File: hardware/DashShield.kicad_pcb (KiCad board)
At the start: 2 copper layers, 112 parts, among them J001 PWR, J101 CAN0, J202 CAN1, J3 Dash LEDs, J301 Steering Wheel, J601 GPIO, Q301 2N7002, Q302 2N7002, Q303 2N7002, Q501 2N7002, Q502 2N7002, Q503 2N7002, Q504 2N7002, Q505 2N7002, Q506 2N7002, U101 MCP2515-xST, U102 MCP2562-E-SN, U201 MCP2515-xST, U202 MCP2562-E-SN, U401 CAT24C256, Y101 8MHz, Y201 8MHz

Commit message: chore: upload progress
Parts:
- added H601: MH, MountingHole:MountingHole_2.7mm_M2.5_Pad, F.Cu at (159.5, 100.0)
- added H602: MH, MountingHole:MountingHole_2.7mm_M2.5_Pad, F.Cu at (217.5, 100.0)
- added H603: MH, MountingHole:MountingHole_2.7mm_M2.5_Pad, F.Cu at (217.5, 149.0)
- added H604: MH, MountingHole:MountingHole_2.7mm_M2.5_Pad, F.Cu at (159.5, 149.0)
- C102, C103, C202, C203: value 22pF -> 16pF
- J601, U101, U102, U201, U202: moved to B.Cu
- Y101, Y201: footprint Crystal:Crystal_SMD_HC49-SD -> Crystal:Crystal_C38-LF_D3.0mm_L8.0mm_Vertical
- moved C105 176.8 mm to (263.0, 145.9), turned to -90 degrees
- moved R104 173.2 mm to (263.8, 141.5), turned to 90 degrees
- moved R103 169.4 mm to (255.8, 147.1)
- moved JP101 163.4 mm to (261.2, 141.2), turned to -90 degrees
- moved JP102 155.6 mm to (258.7, 137.4), turned to 90 degrees
- moved C203 147.7 mm to (234.4, 125.7), turned to -90 degrees
- moved R305 141.6 mm to (210.7, 160.7), turned to -90 degrees
- moved R201 140.8 mm to (225.6, 147.6), turned to 180 degrees
- moved C202 140.5 mm to (232.9, 125.7), turned to 90 degrees
- moved R202 140.3 mm to (225.6, 149.1)
- moved R306 137.8 mm to (210.0, 158.5)
- moved R307 133.8 mm to (204.6, 160.7), turned to 90 degrees
- moved R308 133.1 mm to (206.2, 160.7), turned to -90 degrees
- moved R309 129.3 mm to (205.4, 158.5)
- moved R304 126.0 mm to (209.2, 160.7), turned to 90 degrees
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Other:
- board outline added: 65 x 56.5 mm
- copper layers 2 -> 4

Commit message: Chore-Upload progress
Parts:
- JP101, JP102, JP201, JP202: footprint Connector_PinHeader_2.54mm:PinHeader_1x02_P2.54mm_Vertical -> Jumper:SolderJumper-2_P1.3mm_Open_RoundedPad1.0x1.5mm
- JP401: renamed from JP1; footprint Connector_PinHeader_2.54mm:PinHeader_1x02_P2.54mm_Vertical -> Jumper:SolderJumper-2_P1.3mm_Open_RoundedPad1.0x1.5mm
- moved C104 126.3 mm to (208.0, 142.5), turned to 90 degrees
- moved C101 121.6 mm to (205.5, 129.8), turned to 180 degrees
- moved R13 121.2 mm to (200.1, 137.4), turned to 180 degrees
- moved C401 116.3 mm to (205.4, 121.2)
- moved C205 116.1 mm to (190.5, 141.2), turned to 180 degrees
- moved C201 115.2 mm to (197.6, 143.5), turned to 90 degrees
- moved C204 114.7 mm to (191.0, 135.9), turned to 180 degrees
- moved R204 104.3 mm to (187.2, 144.0), turned to 90 degrees
- moved JP401 96.8 mm to (192.8, 120.5), turned to -90 degrees
- moved R403 94.1 mm to (200.9, 121.2), turned to 180 degrees
- moved R401 90.2 mm to (197.3, 114.6)
- moved R402 90.1 mm to (197.3, 116.8)
- moved C005 83.1 mm to (179.1, 123.7)
- moved C001 79.1 mm to (171.2, 121.7)
- moved C006 79.0 mm to (186.2, 115.6), turned to -90 degrees
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
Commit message: rev2
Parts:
- removed D007: LED, LED_SMD:LED_0603_1608Metric
- added C301: 10nF, Capacitor_SMD:C_0603_1608Metric, F.Cu at (164.4, 133.3)
- added C302: 10nF, Capacitor_SMD:C_0603_1608Metric, F.Cu at (168.3, 136.6)
- added C601: 100nF, Capacitor_SMD:C_0603_1608Metric, F.Cu at (171.3, 134.1)
- added C602: 10nF, Capacitor_SMD:C_0603_1608Metric, F.Cu at (171.3, 130.9)
- added J002: Data Logger, Connector_Molex:Molex_Micro-Fit_3.0_43650-0315_1x03_P3.00mm_Vertical, F.Cu at (189.3, 149.2)
- added U601: ADS1015IDGS, Package_SO:TSSOP-10_3x3mm_P0.5mm, F.Cu at (168.5, 132.6)
- D001, D005: value PMEG3050 -> PMEG100V080ELPD; footprint Diode_SMD:D_SOD-128 -> Package_TO_SOT_SMD:Nexperia_CFP15_SOT-1289
- D006: value PMEG3050 -> LED; footprint Diode_SMD:D_SOD-128 -> LED_SMD:LED_0603_1608Metric
- moved R318 46.7 mm to (157.6, 144.4)
- moved R321 42.0 mm to (157.6, 140.4)
- moved R324 37.2 mm to (157.6, 136.4)
- moved JP201 27.4 mm to (206.8, 144.2)
- moved JP202 24.5 mm to (209.8, 144.2)
- moved J101 23.1 mm to (217.7, 130.6), turned to 90 degrees
- moved R201 20.6 mm to (215.3, 138.8), turned to 0 degrees
- moved C008 20.0 mm to (186.2, 129.1)
- moved R202 19.4 mm to (215.3, 140.6), turned to 180 degrees
- moved U201 18.4 mm to (215.9, 139.7), turned to -90 degrees
- moved R13 18.0 mm to (216.3, 145.2)
- moved Y201 17.7 mm to (211.5, 140.7), turned to 90 degrees
- moved R511 17.6 mm to (209.7, 114.9)
- moved C202 17.6 mm to (211.5, 136.1), turned to 90 degrees
- moved R204 16.6 mm to (203.8, 144.4)
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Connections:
- C003 pad 1: /GPIO3/SCL1 -> /VIN Sense
- C004 pad 1: /GPIO2/SDA1 -> /VBATT Sense
- D001 pad 1: VS -> Net-(J001-Pin_1)
- D001 pad 2: Net-(D001-A) -> Net-(J001-Pin_1)
- D005 pad 1: VS -> +BATT
- D006 pad 1: VS -> GND
- D006 pad 2: +BATT -> Net-(D006-A)
- J001 pad 1: Net-(D001-A) -> Net-(J001-Pin_1)
- R004 pad 1: Net-(D007-A) -> Net-(D006-A)
- R005 pad 1: /GPIO3/SCL1 -> /VIN Sense
- R006 pad 2: /GPIO3/SCL1 -> /VIN Sense
- R007 pad 1: /GPIO2/SDA1 -> /VBATT Sense
- R008 pad 2: /GPIO2/SDA1 -> /VBATT Sense
- R312 pad 1: /GPIO18/PCM.CLK -> /Wheel Slip Adjust
- R315 pad 1: /GPIO23 -> /TC Power Adjust
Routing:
- net GND: track 0.00 -> 129.8 mm, vias 0 -> 23
- net /GPIO10/SPI0.MOSI: track 0.00 -> 82.4 mm
- net /CAN1 INT: track 0.00 -> 81.0 mm, vias 0 -> 1
- net /GPIO11/SPI0.SCLK: track 0.00 -> 69.6 mm, vias 0 -> 2
- net /GPIO9/SPI0.MISO: track 0.00 -> 65.3 mm, vias 0 -> 2
- net /GPIO22: track 0.00 -> 58.9 mm, vias 0 -> 1
- net /GPIO21/PCM.DOUT: track 0.00 -> 58.1 mm, vias 0 -> 1
- net /VIN Sense: track 0.00 -> 57.7 mm, vias 0 -> 4
- net /GPIO7/SPI0.CE1: track 0.00 -> 57.2 mm, vias 0 -> 2
- net /GPIO27: track 0.00 -> 54.2 mm, vias 0 -> 1
- net /GPIO16: track 0.00 -> 53.3 mm, vias 0 -> 1
- net /GPIO20/PCM.DIN: track 0.00 -> 52.5 mm, vias 0 -> 1
- net /CAN0 INT: track 0.00 -> 50.0 mm, vias 0 -> 1
- net /GPIO17: track 0.00 -> 46.9 mm, vias 0 -> 1
- net /GPIO3/SCL1: track 0.00 -> 38.9 mm, vias 0 -> 1
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- added copper zone on In2.Cu, net +5V
- added copper zone on In1.Cu, net GND

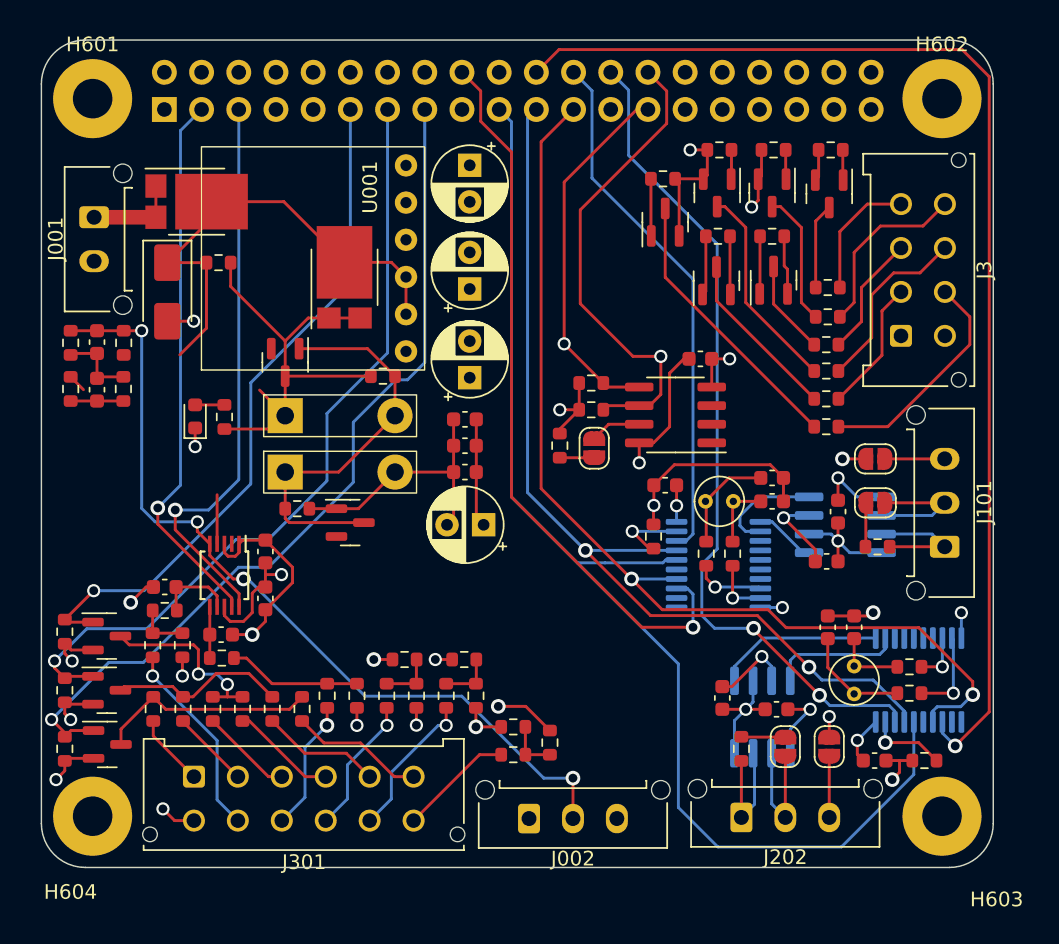
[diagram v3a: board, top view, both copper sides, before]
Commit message: feat: added pours & pass-through for CAN0&CAN1
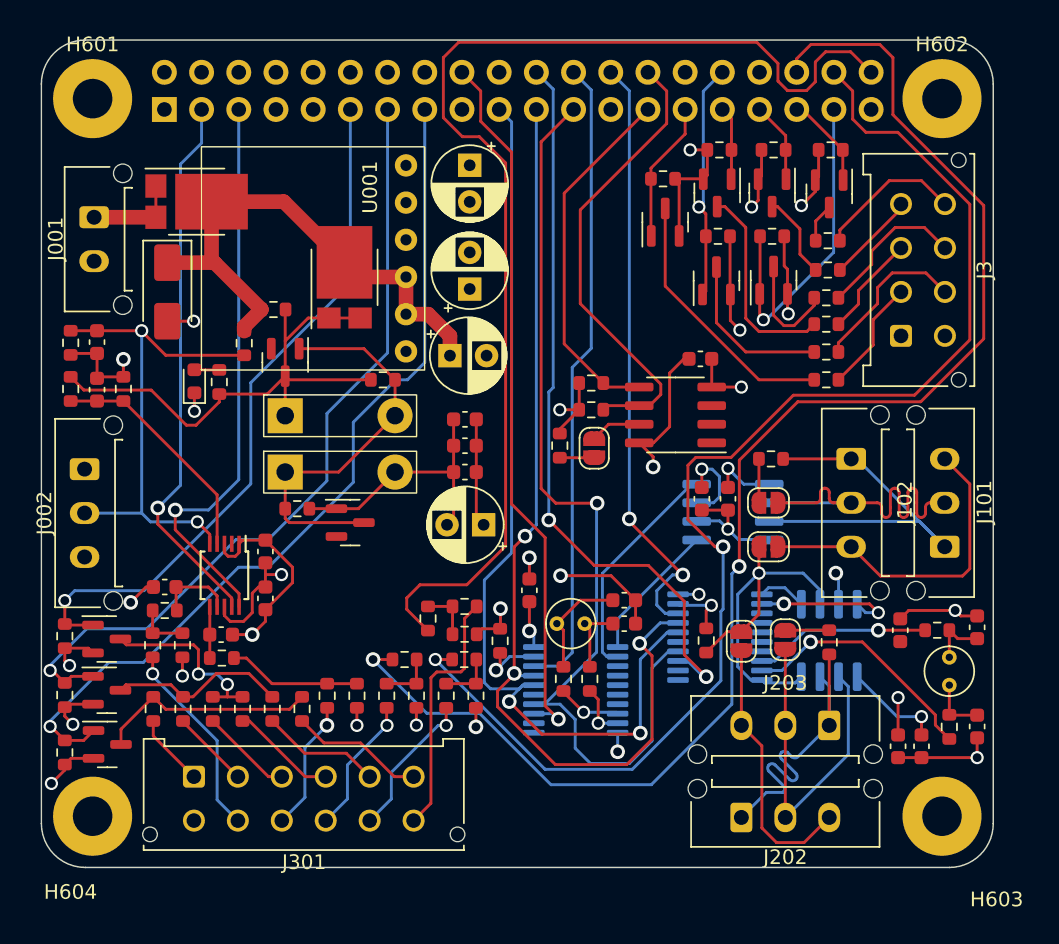
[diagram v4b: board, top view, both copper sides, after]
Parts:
- added J102: CAN0, Connector_Molex:Molex_Micro-Fit_3.0_43650-0315_1x03_P3.00mm_Vertical, F.Cu at (211.3, 124.6)
- added J203: CAN0, Connector_Molex:Molex_Micro-Fit_3.0_43650-0315_1x03_P3.00mm_Vertical, F.Cu at (209.8, 142.8)
- moved J002 38.6 mm to (158.9, 125.3), turned to -90 degrees
- moved R13 17.0 mm to (201.4, 137.0), turned to -90 degrees
- moved U201 13.9 mm to (202.3, 136.8), turned to 180 degrees
- moved Y101 13.1 mm to (193.1, 135.8)
- moved C102 13.1 mm to (195.8, 134.2)
- moved C103 13.1 mm to (195.8, 135.8)
- moved R101 13.0 mm to (191.7, 139.6)
- moved R102 13.0 mm to (193.4, 139.6)
- moved U101 13.0 mm to (192.5, 140.4)
- moved R103 12.7 mm to (187.3, 137.0)
- moved C204 12.4 mm to (214.5, 144.2)
- moved C203 12.2 mm to (219.9, 142.9), turned to 90 degrees
- moved R306 11.9 mm to (182.4, 135.5), turned to 90 degrees
- moved C101 11.7 mm to (189.3, 133.6), turned to 90 degrees
- moved R304 10.7 mm to (184.9, 134.7), turned to 180 degrees
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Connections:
- J3 pad 2: /SLOW LED 0 -> /FAST LED 0
- J3 pad 3: /SLOW LED 1 -> /FAST LED 1
- J3 pad 4: /SLOW LED 2 -> /FAST LED 2
- J3 pad 6: /FAST LED 0 -> /SLOW LED 0
- J3 pad 7: /FAST LED 1 -> /SLOW LED 1
- J3 pad 8: /FAST LED 2 -> /SLOW LED 2
- J601 pad 32: /FAST 2 -> /GPIO12/PWM0
- J601 pad 33: /GPIO13/PWM1 -> /FAST 2
- Q501 pad 1: /GPIO26 -> /GPIO12/PWM0
- Q502 pad 1: /GPIO19/PCM.FS -> /GPIO26
- Q503 pad 1: /GPIO13/PWM1 -> /GPIO19/PCM.FS
- R502 pad 1: /GPIO26 -> /GPIO12/PWM0
- R504 pad 1: /GPIO19/PCM.FS -> /GPIO26
- R506 pad 1: /GPIO13/PWM1 -> /GPIO19/PCM.FS
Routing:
- net /GPIO16: track 53.3 -> 98.7 mm, vias 1 -> 2
- net /GPIO20/PCM.DIN: track 52.5 -> 88.5 mm, vias 1 -> 2
- net /CAN1 INT: track 81.0 -> 50.9 mm, vias 1 -> 2
- net GND: track 129.8 -> 154.4 mm, vias 23 -> 26
- net /GPIO21/PCM.DOUT: track 58.1 -> 81.0 mm, vias 1 -> 0
- net /VIN Sense: track 57.7 -> 34.8 mm, vias 4 -> 2
- net /CAN0 Shield: track 4.09 -> 22.3 mm
- net /GPIO26: track 4.07 -> 22.3 mm, vias 0 -> 1
- net /GPIO10/SPI0.MOSI: track 82.4 -> 64.4 mm, vias 0 -> 2
- net /CAN0 Low: track 8.75 -> 26.7 mm
- net /CAN0 High: track 8.43 -> 26.2 mm
- net /GPIO12/PWM0: track 0.00 -> 16.1 mm, vias 0 -> 1
- net /GPIO7/SPI0.CE1: track 57.2 -> 41.2 mm
- net /CAN1 High: track 8.58 -> 23.3 mm
- net /CAN1 Shield: track 4.19 -> 18.4 mm
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- added copper zone on In2.Cu, net +3.3V
- removed copper zone on In2.Cu, net +5V

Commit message: chore: add all LCSC parts and update footprints
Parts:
- C005, C007, C008: footprint Capacitor_THT:CP_Radial_D5.0mm_P2.50mm -> Capacitor_SMD:C_0603_1608Metric
- C006: footprint Capacitor_THT:CP_Radial_D5.0mm_P2.50mm -> Capacitor_SMD:C_1206_3216Metric
- C102, C103, C202, C203: value 16pF -> 10pF
- D006: value LED -> BATT LED
- R001: value 3.3 -> 13; footprint Resistor_SMD:R_0603_1608Metric -> Resistor_SMD:R_2512_6332Metric
- R310, R313: value 500 -> 470
- U101, U201: value MCP2515-xST -> MCP2515-I/ST
- Y101, Y201: footprint Crystal:Crystal_C38-LF_D3.0mm_L8.0mm_Vertical -> Crystal:Crystal_SMD_Abracon_ABM3B-4Pin_5.0x3.2mm
- moved C003 61.9 mm to (110.1, 79.7)
- moved C004 61.9 mm to (110.1, 82.9)
- moved C009 61.9 mm to (135.3, 88.6)
- moved C010 61.9 mm to (135.3, 86.8)
- moved C011 61.9 mm to (135.3, 85.0)
- moved C102 61.9 mm to (146.1, 97.3)
- moved C201 61.9 mm to (165.0, 99.4)
- moved C203 61.9 mm to (170.2, 105.9)
- moved C601 61.9 mm to (121.6, 97.2)
- moved C602 61.9 mm to (121.6, 94.0)
- moved J202 61.9 mm to (154.1, 112.1)
- moved J203 61.9 mm to (160.1, 105.9)
- moved JP202 61.9 mm to (154.1, 100.1)
- moved Q503 61.9 mm to (160.1, 69.6)
- moved Q505 61.9 mm to (152.5, 69.5)
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
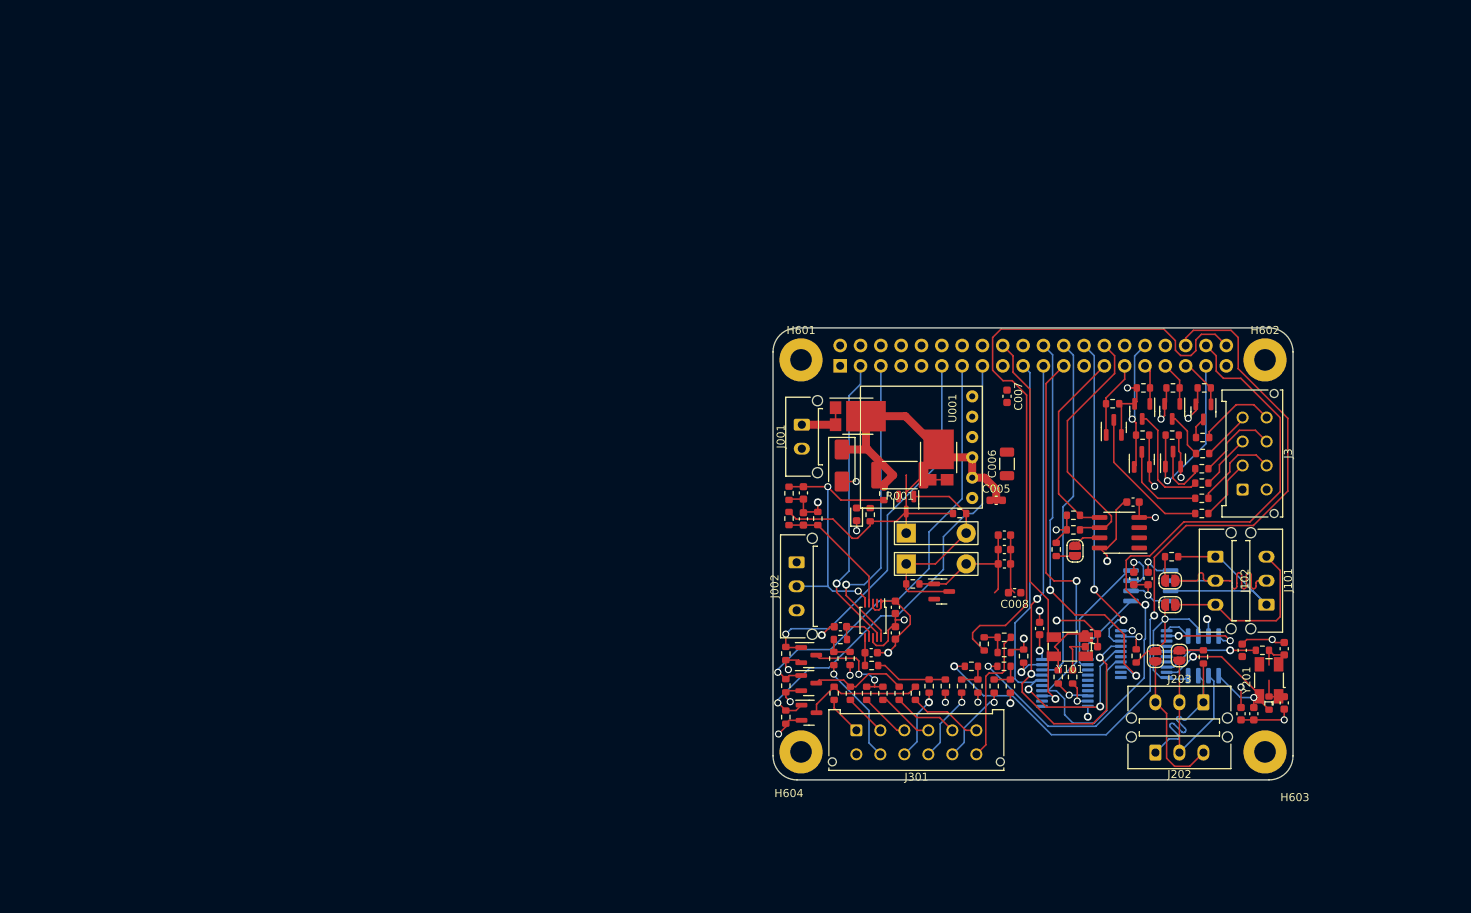
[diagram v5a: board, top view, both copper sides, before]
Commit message: chore: I2C pullups and new WIP layout
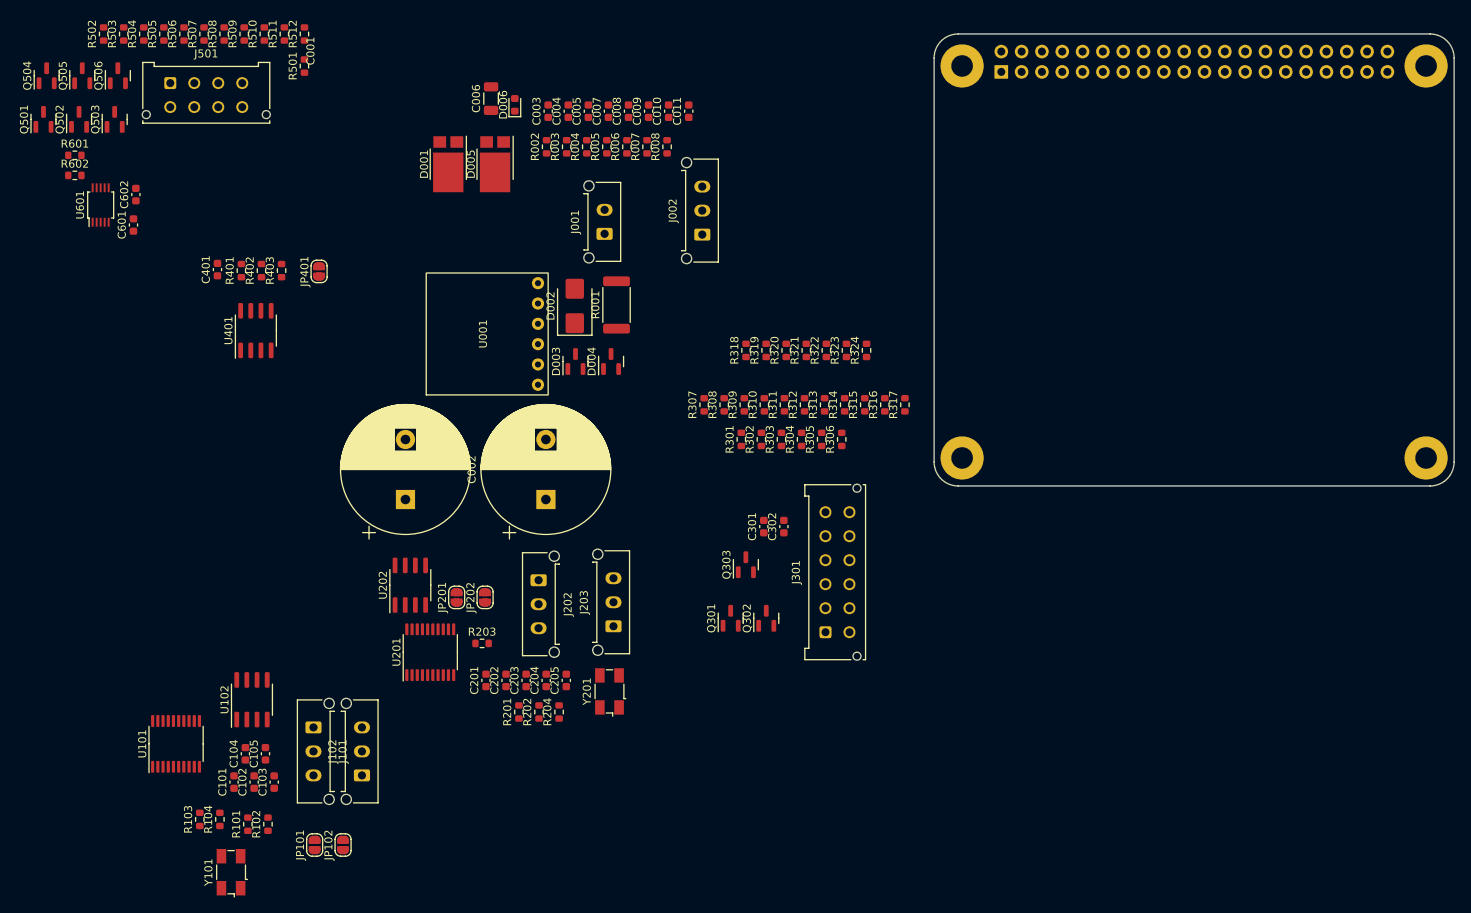
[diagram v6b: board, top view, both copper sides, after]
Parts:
- removed J3: Dash LEDs, Connector_Molex:Molex_Micro-Fit_3.0_43045-0812_2x04_P3.00mm_Vertical
- removed R13: 4k7, Resistor_SMD:R_0603_1608Metric
- added J501: Dash LEDs, Connector_Molex:Molex_Micro-Fit_3.0_43045-0812_2x04_P3.00mm_Vertical, F.Cu at (31.0, 28.5)
- added R203: 4k7, Resistor_SMD:R_0603_1608Metric, F.Cu at (70.0, 98.5)
- added R601: 3k9, Resistor_SMD:R_0603_1608Metric, F.Cu at (19.1, 37.5)
- added R602: 3k9, Resistor_SMD:R_0603_1608Metric, F.Cu at (19.1, 40.0)
- D002: footprint Diode_SMD:D_SMA -> Diode_SMD:D_SMB
- D003, D004: value 2.7V -> 2.4V
- R001: value 13 -> 47
- U101, U102, U201, U202: moved to F.Cu
- moved R503 145.3 mm to (25.2, 22.3), turned to 90 degrees
- moved Q501 143.7 mm to (15.2, 33.0)
- moved Q502 143.2 mm to (19.6, 33.0)
- moved Q503 140.9 mm to (24.1, 33.0), turned to 90 degrees
- moved Q504 140.5 mm to (15.6, 27.5)
- moved R505 139.3 mm to (30.2, 22.3), turned to 90 degrees
- moved R502 139.2 mm to (22.7, 22.3), turned to 90 degrees
- moved Q505 139.0 mm to (20.0, 27.5), turned to 90 degrees
- moved R507 138.4 mm to (35.2, 22.3), turned to 90 degrees
- moved Q506 138.3 mm to (24.4, 27.5), turned to 90 degrees
- moved R504 138.0 mm to (27.7, 22.3), turned to 90 degrees
- moved R506 135.0 mm to (32.7, 22.3), turned to 90 degrees
- moved R509 132.2 mm to (40.2, 22.3), turned to 90 degrees
- moved R511 126.2 mm to (45.3, 22.3), turned to 90 degrees
- moved R501 124.5 mm to (47.8, 26.3), turned to 90 degrees
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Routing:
- net GND: track 154.4 -> 0.00 mm, vias 26 -> 0
- net /GPIO16: track 98.7 -> 0.00 mm, vias 2 -> 0
- net /GPIO20/PCM.DIN: track 88.5 -> 0.00 mm, vias 2 -> 0
- net /GPIO21/PCM.DOUT: track 81.0 -> 0.00 mm
- net /GPIO9/SPI0.MISO: track 66.3 -> 0.00 mm, vias 3 -> 0
- net /GPIO11/SPI0.SCLK: track 65.8 -> 0.00 mm, vias 1 -> 0
- net /GPIO10/SPI0.MOSI: track 64.4 -> 0.00 mm, vias 2 -> 0
- net /GPIO22: track 59.4 -> 0.00 mm, vias 1 -> 0
- net /GPIO27: track 55.0 -> 0.00 mm, vias 1 -> 0
- net /CAN1 INT: track 50.9 -> 0.00 mm, vias 2 -> 0
- net /CAN0 INT: track 48.7 -> 0.00 mm, vias 1 -> 0
- net /GPIO17: track 47.9 -> 0.00 mm, vias 1 -> 0
- net /GPIO8/SPI0.CE0: track 43.7 -> 0.00 mm
- net /GPIO7/SPI0.CE1: track 41.2 -> 0.00 mm, vias 2 -> 0
- net +3.3V: track 39.3 -> 0.00 mm, vias 7 -> 0
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- removed copper zone on In2.Cu, net +3.3V
- removed copper zone on In1.Cu, net GND
